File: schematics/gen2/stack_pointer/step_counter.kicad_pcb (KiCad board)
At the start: 2 copper layers, 100 x 89.5 mm, 16 parts, among them U1 74HC00, U2 74HC193, U3 74HC193, U4 74HC193, U5 74HC193, U6 74HC245, U7 74HC245

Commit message: stack rework
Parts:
- removed C1, C2, C3, C4, C5, C6, C7, C8: C, Capacitor_SMD:C_0805_2012Metric_Pad1.18x1.45mm_HandSolder
- moved U5 66.2 mm to (176.4, 67.4)
- moved U3 65.6 mm to (176.6, 51.4)
- moved U4 45.3 mm to (130.7, 67.6)
- moved U7 33.6 mm to (160.0, 95.9)
- moved U6 31.6 mm to (160.0, 112.1)
- moved U2 16.4 mm to (130.9, 51.7)
- moved U1 7.23 mm to (200.0, 108.2), turned to 180 degrees
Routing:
- net VCC: track 473.6 -> 50.8 mm
- net GND: track 371.7 -> 143.6 mm, vias 22 -> 8
- net /Pl: track 75.9 -> 164.0 mm, vias 0 -> 2
- net /DATA0: track 200.1 -> 114.5 mm, vias 1 -> 2
- net /DATA2: track 182.1 -> 98.1 mm, vias 1 -> 0
- net /DATA7: track 174.5 -> 96.7 mm
- net /DATA5: track 154.7 -> 82.5 mm, vias 1 -> 0
- net /DATA4: track 163.6 -> 92.6 mm, vias 1 -> 2
- net /DATA1: track 180.8 -> 110.1 mm, vias 1 -> 0
- net /DATA3: track 167.9 -> 98.1 mm, vias 1 -> 0
- net /RESET: track 145.5 -> 213.6 mm, vias 1 -> 2
- net /CPu: track 63.9 -> 130.6 mm, vias 0 -> 3
- net /CPd: track 69.8 -> 133.6 mm, vias 0 -> 3
- net Net-(U2-~{BO}): track 27.0 -> 89.3 mm, vias 0 -> 2
- net /DATA6: track 158.0 -> 96.1 mm
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- added copper zone on F.Cu, net VCC
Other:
- board size 100 x 89.5 mm -> 100 x 91 mm

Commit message: update
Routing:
- net VCC: track 50.8 -> 27.3 mm
- net GND: track 143.6 -> 121.5 mm, vias 8 -> 9
- net /Pl: track 164.0 -> 161.5 mm
- net Net-(U2-~{CO}): track 87.4 -> 86.7 mm
- net /RESET: track 213.6 -> 212.9 mm
- net /PULSE: track 48.0 -> 47.4 mm

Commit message: complete stack
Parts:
- added C1: C, Capacitor_THT:C_Radial_D6.3mm_H5.0mm_P2.50mm, F.Cu at (116.5, 117.8)
- added C2: C, Capacitor_THT:C_Disc_D3.0mm_W1.6mm_P2.50mm, F.Cu at (124.0, 44.0)
- added C3: C, Capacitor_THT:C_Disc_D3.0mm_W1.6mm_P2.50mm, F.Cu at (192.5, 114.2)
- added C4: C, Capacitor_THT:C_Disc_D3.0mm_W1.6mm_P2.50mm, F.Cu at (169.5, 44.0)
- added C5: C, Capacitor_THT:C_Disc_D3.0mm_W1.6mm_P2.50mm, F.Cu at (124.0, 60.0)
- added C6: C, Capacitor_THT:C_Disc_D3.0mm_W1.6mm_P2.50mm, F.Cu at (169.5, 60.0)
- added C7: C, Capacitor_THT:C_Disc_D3.0mm_W1.6mm_P2.50mm, F.Cu at (155.5, 104.5)
- added C8: C, Capacitor_THT:C_Disc_D3.0mm_W1.6mm_P2.50mm, F.Cu at (155.5, 88.0)
- moved U3 0.41 mm to (176.5, 51.8)
- moved U5 0.38 mm to (176.5, 67.8)
- moved U2 0.29 mm to (130.6, 51.8)
- moved U1 0.28 mm to (200.1, 108.5)
- moved U4 0.24 mm to (130.6, 67.8)
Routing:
- net /CPu: track 130.6 -> 92.8 mm, vias 3 -> 2
- net VCC: track 27.3 -> 61.4 mm
- net /CPd: track 133.6 -> 103.2 mm, vias 3 -> 2
- net GND: track 121.5 -> 127.8 mm
- net /DL3: track 48.0 -> 54.0 mm
- net /DL2: track 48.0 -> 53.8 mm
- net /~{RSPH}: track 58.4 -> 55.0 mm
- net /DH4: track 51.3 -> 49.0 mm
- net /RESET: track 212.9 -> 214.4 mm
- net /DL5: track 45.9 -> 47.0 mm
- net /~{CLK}: track 39.9 -> 38.9 mm
- net /PULSE: track 47.4 -> 46.5 mm
- net /Ph: track 115.2 -> 115.9 mm
- net /Pl: track 161.5 -> 162.2 mm
- net Net-(U2-UP): track 53.4 -> 54.1 mm
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
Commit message: design + fix core_2
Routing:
- net /DL5: track 47.0 -> 47.1 mm, vias 0 -> 2
- net /DL6: vias 0 -> 2
- net /Ph: vias 0 -> 2
- net /DL4: vias 0 -> 2
- net /Pl: vias 2 -> 4
- net /DH6: vias 0 -> 2
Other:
- board text removed: "DRAGONFLY"

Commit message: update core_2
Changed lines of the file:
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@@
 	)
 	(segment
-		(start 189.5 126.5)
-		(end 203.5 112.5)
-		(width 0.2)
-		(layer "F.Cu")
-		(net 8)
-	)
-	(segment
-		(start 203.5 112.5)
-		(end 203.5 101.72)
-		(width 0.2)
-		(layer "F.Cu")
-		(net 8)
-	)
-	(segment
-		(start 203.5 101.72)
+		(start 204 102.22)
 		(end 200.12 98.34)
 		(width 0.2)
@@
 	)
 	(segment
+		(start 204 112)
+		(end 204 102.22)
+		(width 0.2)
+		(layer "F.Cu")
+		(net 8)
+	)
+	(segment
 		(start 189.5 130)
 		(end 189.5 126.5)
@@
 	)
 	(segment
+		(start 189.5 126.5)
+		(end 204 112)
+		(width 0.2)
+		(layer "F.Cu")
+		(net 8)
+	)
+	(segment
 		(start 200.12 109.88)
 		(end 200.12 108.5)
@@
 		(start 203 108.84)
 		(end 200.12 105.96)
-		(width 0.3)
+		(width 0.4)
 		(layer "F.Cu")
 		(net 111)
@@
 		(start 200.12 105.96)
 		(end 192.5 105.96)
-		(width 0.3)
+		(width 0.4)
 		(layer "F.Cu")
 		(net 111)
@@
 		(start 188.5 126)
 		(end 203 111.5)
-		(width 0.3)
+		(width 0.4)
 		(layer "F.Cu")
 		(net 111)
@@
 		(start 188.5 130)
 		(end 188.5 126)
-		(width 0.3)
+		(width 0.4)
 		(layer "F.Cu")
 		(net 111)
@@
 		(start 203 111.5)
 		(end 203 108.84)
-		(width 0.3)
+		(width 0.4)
 		(layer "F.Cu")
 		(net 111)

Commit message: fix(stack pointer): fixed footprints
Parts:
- added kibuzzard-6911C575: G***, kibuzzard-6911C575, F.Cu at (119.6, 38.9)
- C2, C3, C4, C5, C6, C7, C8: footprint Capacitor_THT:C_Disc_D3.0mm_W1.6mm_P2.50mm -> Capacitor_THT:C_Disc_D5.0mm_W2.5mm_P5.00mm
- moved C3 93.1 mm to (126.3, 48.8)
- moved C5 47.0 mm to (168.2, 44.2)
- moved C8 46.0 mm to (193.4, 114.1)
- moved C6 31.3 mm to (152.2, 86.0)
- moved C2 20.8 mm to (125.8, 64.8), turned to 90 degrees
- moved C4 16.0 mm to (166.7, 59.8)
- moved C1 1.46 mm to (116.3, 116.3)
- moved C7 0.89 mm to (156.2, 104.0)
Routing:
- net VCC: track 61.4 -> 65.4 mm
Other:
- board text removed: "STACK POINTER"

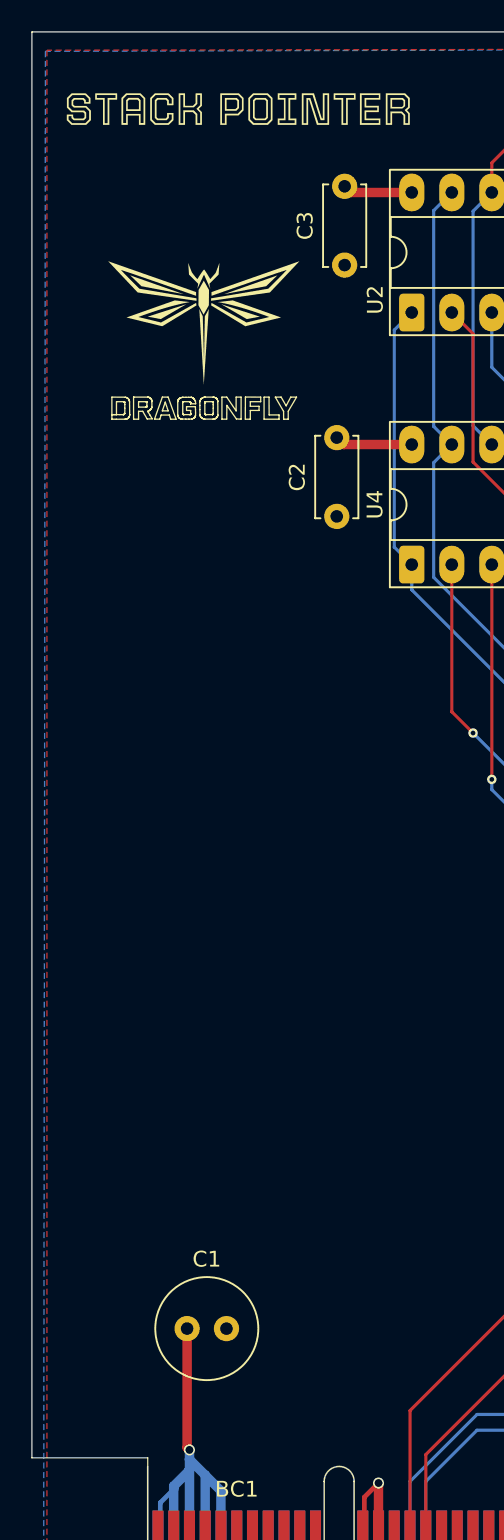
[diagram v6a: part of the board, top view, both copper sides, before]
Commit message: chore(kicad-pcb): added apps ucu logo
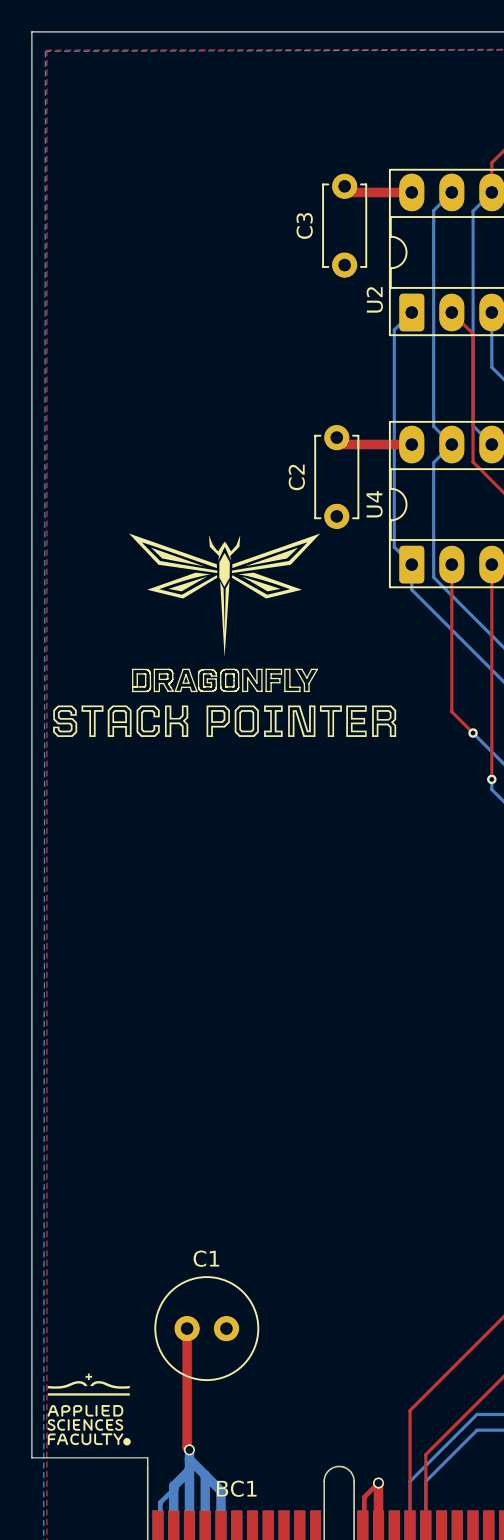
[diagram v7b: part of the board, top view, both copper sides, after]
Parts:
- moved kibuzzard-6911C575 38.9 mm to (118.7, 77.8)

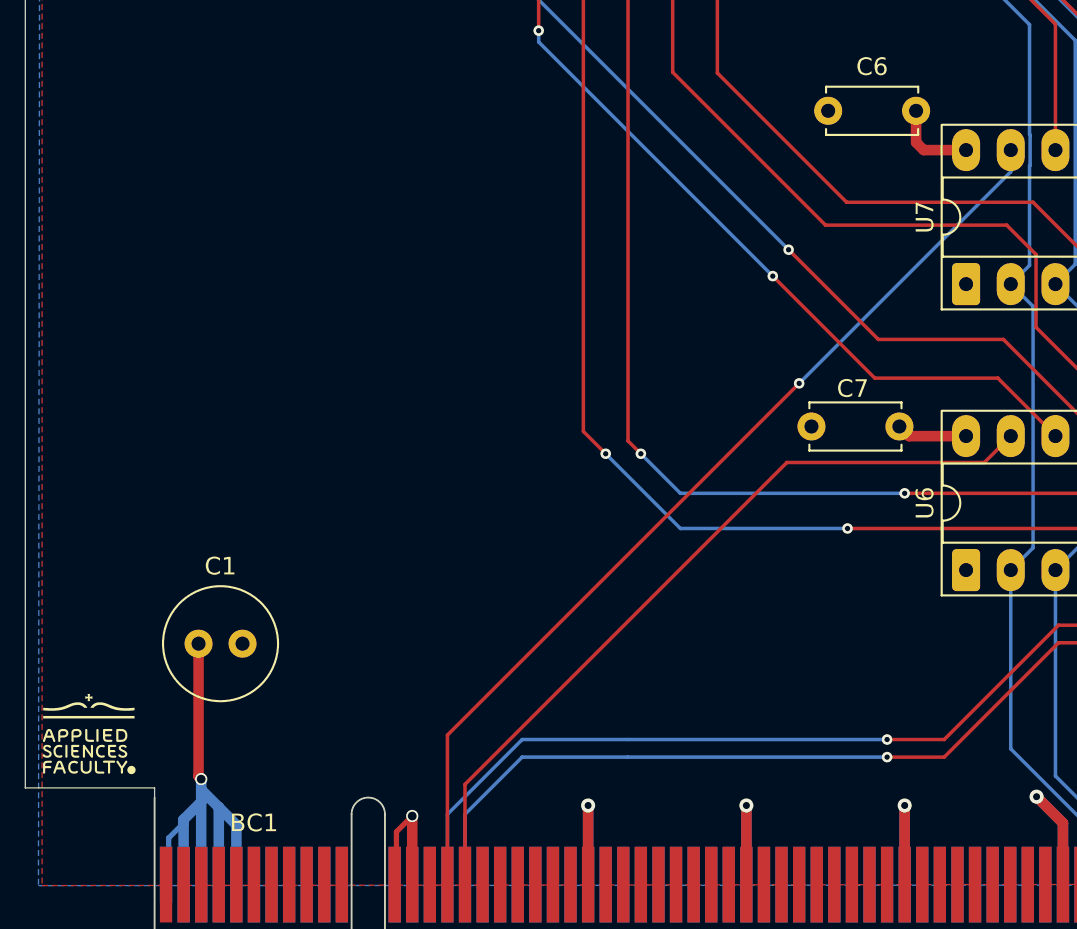
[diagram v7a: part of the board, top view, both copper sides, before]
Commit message: changes pc sc interface
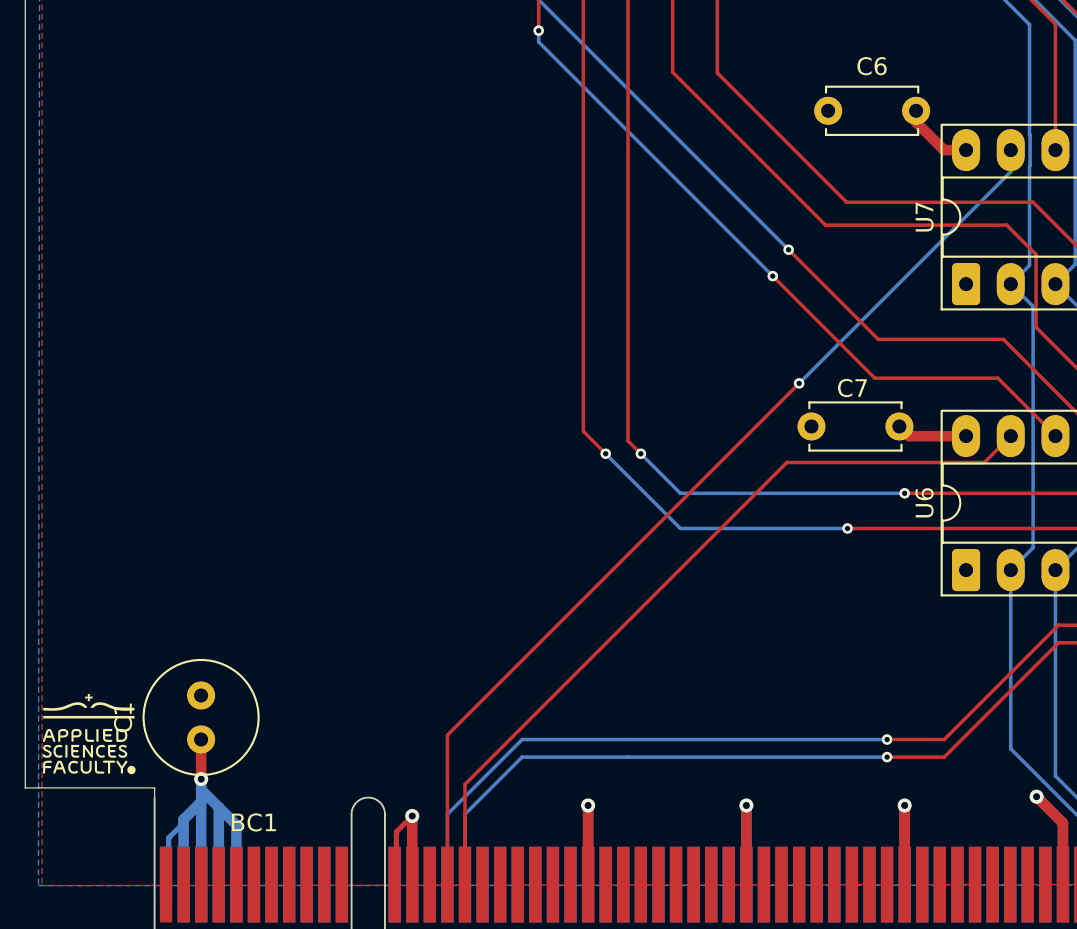
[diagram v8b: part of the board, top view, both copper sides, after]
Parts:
- moved C1 5.45 mm to (116.5, 121.7), turned to 90 degrees
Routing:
- net VCC: track 65.4 -> 59.3 mm
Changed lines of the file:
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@@
 			(pinfunction "VCC")
 			(pintype "power_in")
+			(zone_connect 0)
 		)
 		(embedded_fonts no)
@@
 			(pinfunction "VCC")
 			(pintype "power_in")
+			(zone_connect 0)
 		)
 		(embedded_fonts no)
@@
 			(pinfunction "VCC")
 			(pintype "power_in")
+			(zone_connect 0)
 		)
 		(embedded_fonts no)
@@
 	(footprint "Capacitor_THT:C_Radial_D6.3mm_H5.0mm_P2.50mm"
 		(layer "F.Cu")
-		(at 116.35 116.3)
+		(at 116.49498 121.746451 90)
 		(descr "C, Radial series, Radial, pin pitch=2.50mm, diameter=6.3mm, height=5mm, Non-Polar Electrolytic Capacitor")
 		(tags "C Radial series Radial pin pitch 2.50mm diameter 6.3mm height 5mm Non-Polar Electrolytic Capacitor")
 		(property "Reference" "C1"
-			(at 1.25 -4.4 0)
+			(at 1.25 -4.4 90)
 			(layer "F.SilkS")
 			(effects
@@
 		)
 		(property "Value" "C"
-			(at 1.25 4.4 0)
+			(at 1.25 4.4 90)
 			(layer "F.Fab")
 			(effects
@@
 		)
 		(property "Datasheet" "~"
-			(at 0 0 0)
+			(at 0 0 90)
 			(layer "F.Fab")
 			(hide yes)
@@
 		)
 		(property "Description" "Unpolarized capacitor"
-			(at 0 0 0)
+			(at 0 0 90)
 			(layer "F.Fab")
 			(hide yes)
@@
 		)
 		(fp_text user "${REFERENCE}"
-			(at 1.25 0 0)
+			(at 1.25 0 90)
 			(layer "F.Fab")
 			(effects
@@
 		)
 		(pad "1" thru_hole circle
-			(at 0 0)
+			(at 0 0 90)
 			(size 1.6 1.6)
 			(drill 0.8)
@@
 		)
 		(pad "2" thru_hole circle
-			(at 2.5 0)
+			(at 2.5 0 90)
 			(size 1.6 1.6)
 			(drill 0.8)
@@
 			(pinfunction "VCC")
 			(pintype "power_in")
+			(zone_connect 0)
 		)
 		(embedded_fonts no)
@@
 			(pinfunction "VCC")
 			(pintype "power_in")
+			(zone_connect 0)
 		)
 		(embedded_fonts no)
@@
 			(pinfunction "VCC")
 			(pintype "power_in")
+			(zone_connect 0)
 		)
 		(embedded_fonts no)
@@
 			(pinfunction "VCC")
 			(pintype "power_in")
+			(zone_connect 0)
 		)
 		(embedded_fonts no)
@@
 	)
 	(segment
-		(start 159.992254 88.234777)
-		(end 157.584777 88.234777)
-		(width 0.6)
-		(layer "F.Cu")
-		(net 1)
-	)
-	(segment
-		(start 157.15 87.8)
+		(start 157.15 86.65)
 		(end 157.15 86)
 		(width 0.6)
@@
 	)
 	(segment
+		(start 116.5 124)
+		(end 116.5 121.751471)
+		(width 0.6)
+		(layer "F.Cu")
+		(net 1)
+	)
+	(segment
 		(start 126.35 43.8)
 		(end 126.74 44.19)
@@
 	)
 	(segment
-		(start 116.5 124)
-		(end 116.35 123.85)
+		(start 130.61 60.19)
+		(end 126.29 60.19)
 		(width 0.6)
 		(layer "F.Cu")
@@
 	)
 	(segment
-		(start 130.61 60.19)
-		(end 126.29 60.19)
+		(start 172.85 60.2)
+		(end 172.1 60.2)
 		(width 0.6)
 		(layer "F.Cu")
@@
 	)
 	(segment
-		(start 116.35 123.85)
-		(end 116.35 116.3)
+		(start 176.46 60.19)
+		(end 172.86 60.19)
 		(width 0.6)
 		(layer "F.Cu")
@@
 	)
 	(segment
-		(start 157.584777 88.234777)
-		(end 157.15 87.8)
+		(start 158.734777 88.234777)
+		(end 157.15 86.65)
 		(width 0.6)
 		(layer "F.Cu")
@@
 	)
 	(segment
-		(start 172.85 60.2)
-		(end 172.1 60.2)
-		(width 0.6)
+		(start 173.26 44.19)
+		(end 173.25 44.2)
+		(width 0.2)
 		(layer "F.Cu")
 		(net 1)
 	)
 	(segment
-		(start 176.46 60.19)
-		(end 172.86 60.19)
+		(start 116.5 121.751471)
+		(end 116.49498 121.746451)
 		(width 0.6)
 		(layer "F.Cu")
@@
 	)
 	(segment
-		(start 173.26 44.19)
-		(end 173.25 44.2)
-		(width 0.2)
+		(start 126.29 60.19)
+		(end 125.85 59.75)
+		(width 0.6)
 		(layer "F.Cu")
 		(net 1)
 	)
 	(segment
-		(start 126.29 60.19)
-		(end 125.85 59.75)
+		(start 159.992254 88.234777)
+		(end 158.734777 88.234777)
 		(width 0.6)
 		(layer "F.Cu")
@@
 	(via
 		(at 116.5 124)
-		(size 0.7)
-		(drill 0.5)
+		(size 0.8)
+		(drill 0.4)
 		(layers "F.Cu" "B.Cu")
 		(free yes)
@@
 	(via
 		(at 128.5 126.1)
-		(size 0.7)
-		(drill 0.5)
+		(size 0.8)
+		(drill 0.4)
 		(layers "F.Cu" "B.Cu")
 		(free yes)
